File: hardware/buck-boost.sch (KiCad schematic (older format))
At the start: 60 parts, among them J1 FC681465, J2 Screw_Terminal_1x02, J3 Screw_Terminal_1x02, J4 DS1013-20S, J5 PLS-2, Q1 IRLML0030TRPBF, SW1 SW_Push, U1 L78L33_SOT89, Y1 Crystal

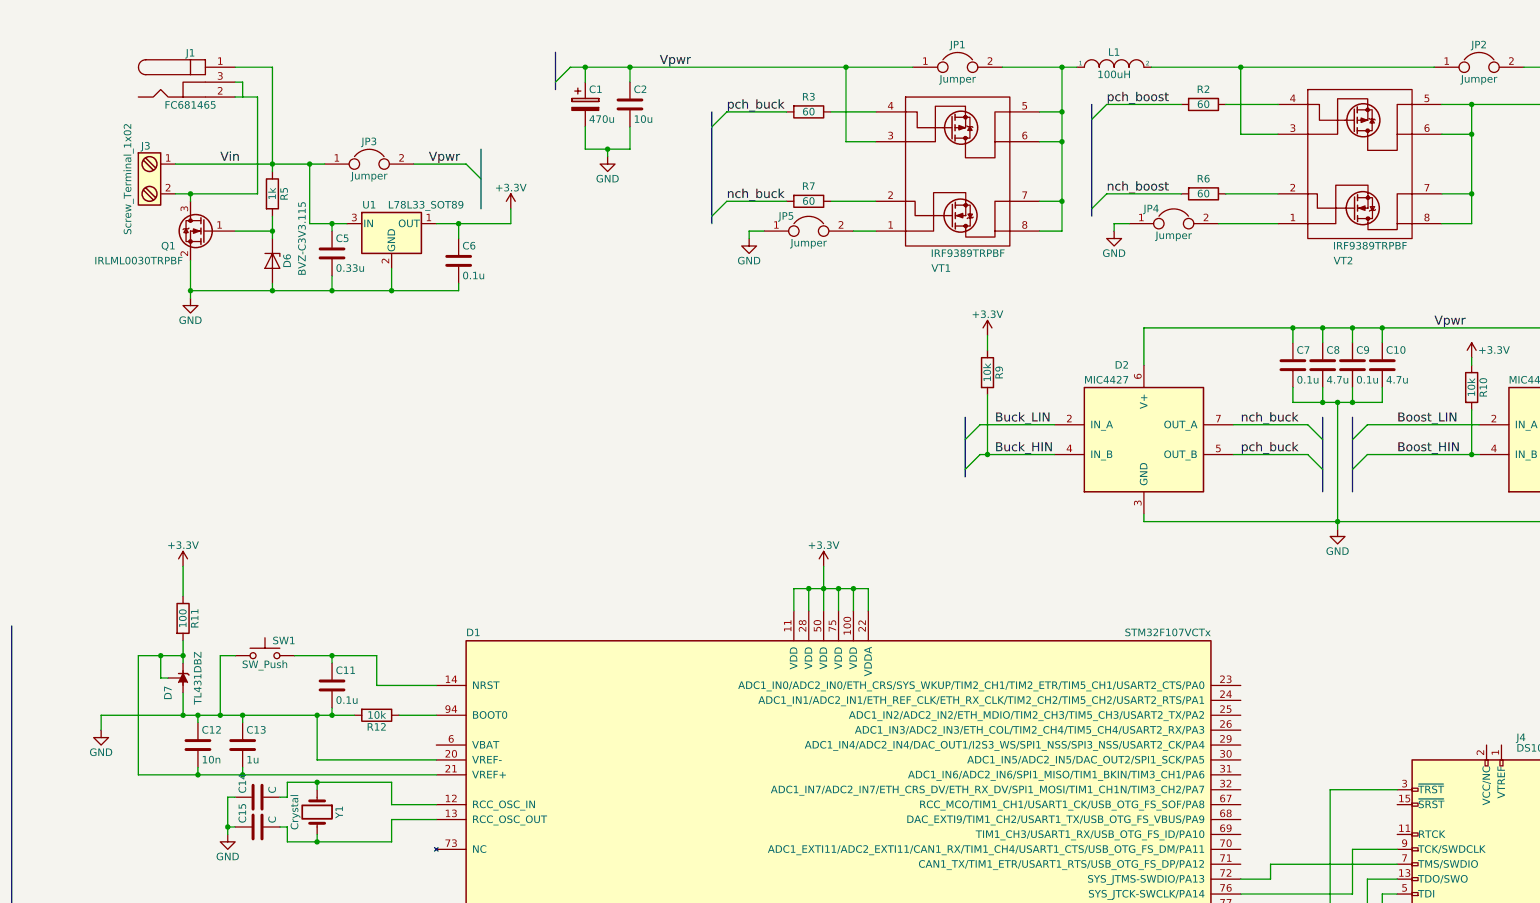
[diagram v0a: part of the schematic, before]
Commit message: fix schematic + set footprints
fix a few issues in schematic and set footprints for all components
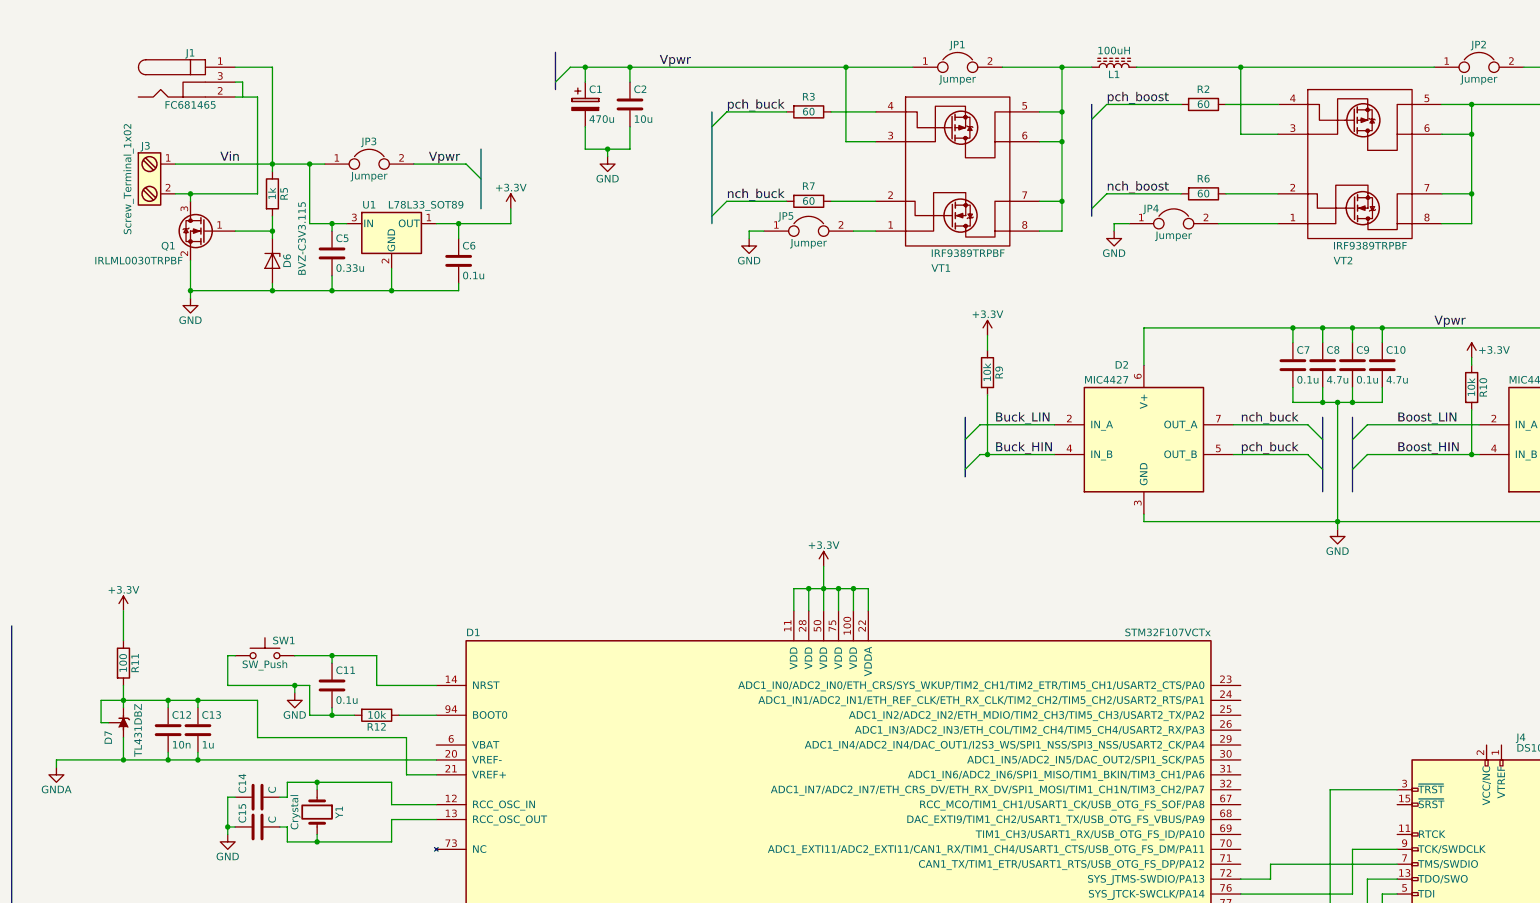
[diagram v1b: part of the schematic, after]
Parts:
- removed L1: 100uH, symbol INDUCTOR
- added L1: 100uH, Inductors_SMD:INDUCTOR_Bourns_SDR1307, symbol L_Core_Ferrite
- C1, C3: footprint (none) -> Capacitors_THT:CP_Radial_D10.0mm_P5.00mm
- C10, C23, C8: footprint (none) -> Capacitors_SMD:C_1206_HandSoldering
- C11, C12, C13, C14, C15, C16, C17, C18, C19, C20, C21, C22, C5, C6, C7, C9: footprint (none) -> Capacitors_SMD:C_0603_HandSoldering
- C2, C4: footprint (none) -> Capacitors_SMD:C_1210_HandSoldering
- D1: footprint LQFP100 -> Housings_QFP:LQFP-100_14x14mm_Pitch0.5mm
- D2, D3: footprint (none) -> Housings_SOIC:SOIC-8_3.9x4.9mm_Pitch1.27mm
- D4: footprint Package_TO_SOT_SMD:SOT-23-5 -> TO_SOT_Packages_SMD:SOT-23-5_HandSoldering
- D5: footprint TO_SOT_Packages_SMD:SOT-23-5 -> TO_SOT_Packages_SMD:SOT-23-5_HandSoldering
- D6: footprint (none) -> Diodes_SMD:D_1206
- D7, Q1: footprint Package_TO_SOT_SMD:SOT-23 -> TO_SOT_Packages_SMD:SOT-23
- J1: footprint (none) -> Connectors:BARREL_JACK
- J2, J3: footprint (none) -> TerminalBlock_Phoenix:TerminalBlock_Phoenix_MKDS1.5-2pol
- J4: footprint (none) -> Connectors:IDC_Header_Straight_20pins
- J5, JP1, JP2, JP3, JP4, JP5: footprint (none) -> Pin_Headers:Pin_Header_Straight_1x02_Pitch2.54mm
- R1: footprint (none) -> Resistors_SMD:R_1206_HandSoldering
- R10, R11, R12, R13, R4, R5, R8, R9: footprint (none) -> Resistors_SMD:R_0603_HandSoldering
- R2, R3, R6, R7: footprint (none) -> Resistors_SMD:R_0805_HandSoldering
- SW1: footprint (none) -> Buttons_Switches_THT:SW_PUSH_6mm
- U1: footprint Package_TO_SOT_SMD:SOT-89-3 -> TO_SOT_Packages_SMD:SOT-89-3_Handsoldering
- VT1, VT2: footprint Housings_SOIC:SO-8_5.3x6.2mm_Pitch1.27mm -> Housings_SOIC:SOIC-8_3.9x4.9mm_Pitch1.27mm
- Y1: footprint (none) -> Crystals:Crystal_HC49-U_Vertical
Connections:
- net GND: no longer C12.1, C13.1, D1.20 (VREF-), D7.3 (A)
- net GNDA: now also C12.2, C13.2, D1.20 (VREF-), D7.3 (A)
- net at JP1.2, VT1.5 (D2), VT1.6 (D2)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: now also L1.1
- net at JP2.1, VT2.3 (S2): now also L1.2
- net at D1.21 (VREF+), D7.1 (K), D7.2 (REF)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: now also C12.1, C13.1; no longer C12.2, C13.2
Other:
- moved on the sheet: C12, C13, D7, R11

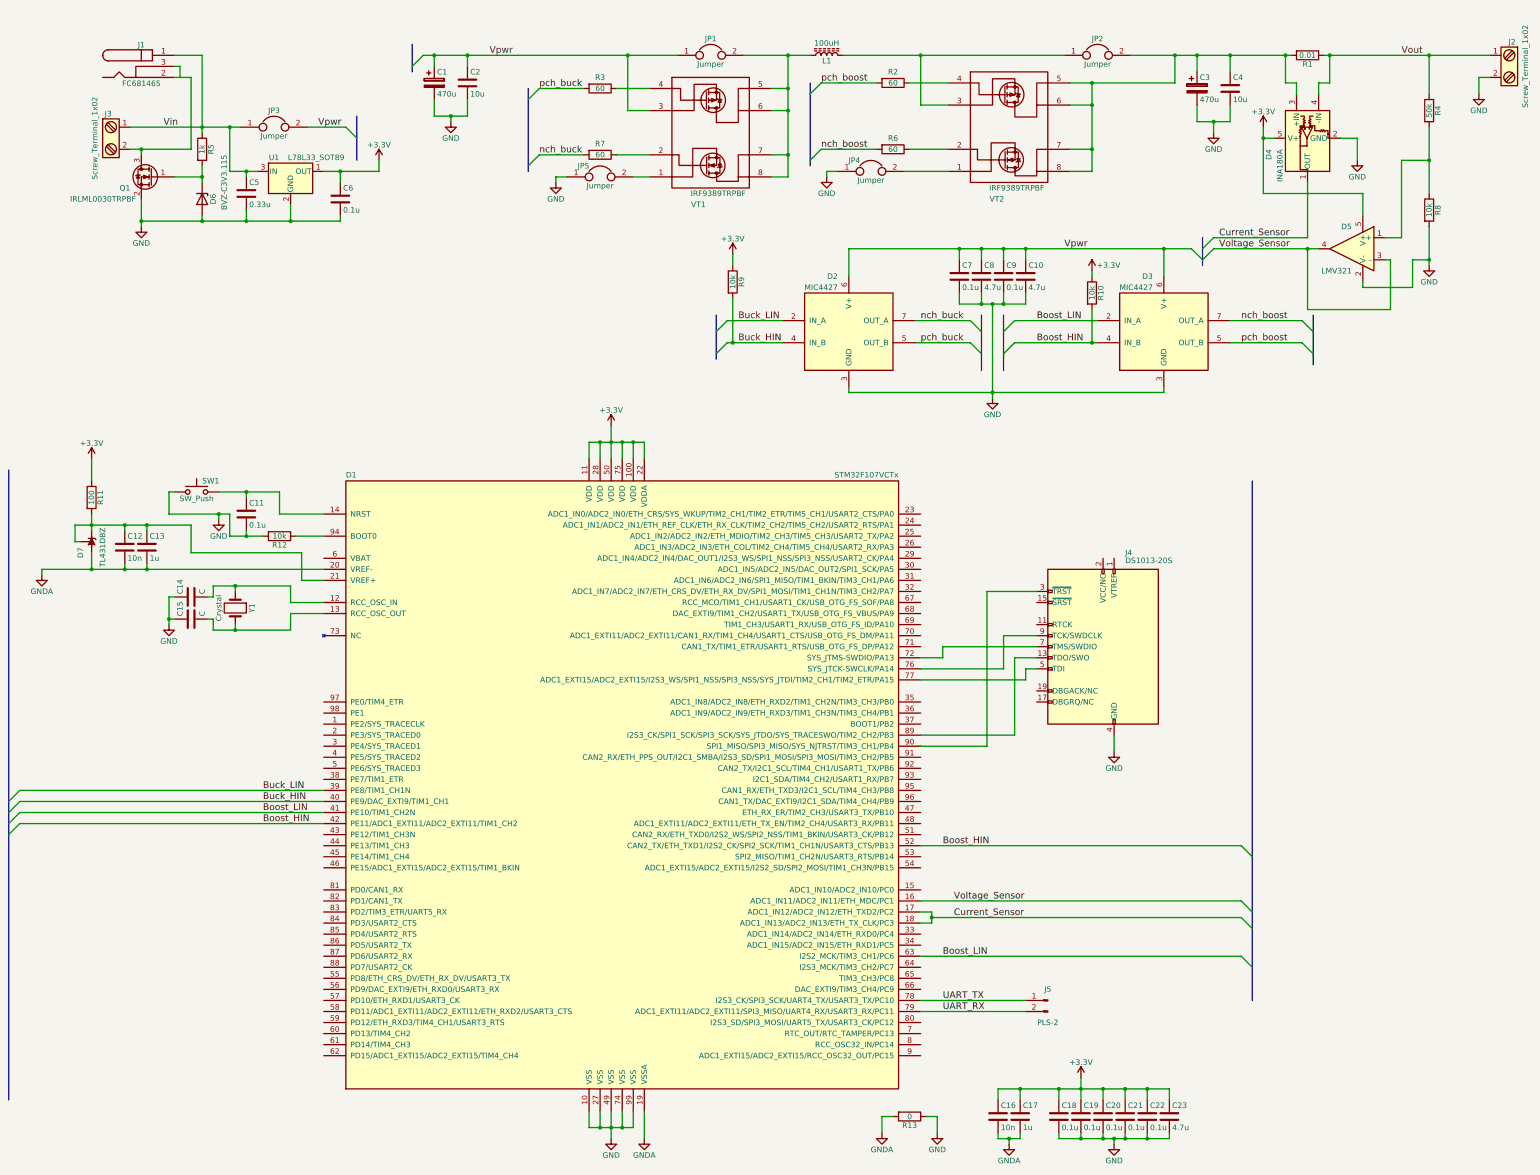
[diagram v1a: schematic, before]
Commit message: add pcb to project(first version) and schematic changes
Schematic
1. Test points added
2. Reset button and GNDA deleted
3. Voltage and Current sensors inputs on MCU (D1) was changed for better PCB design
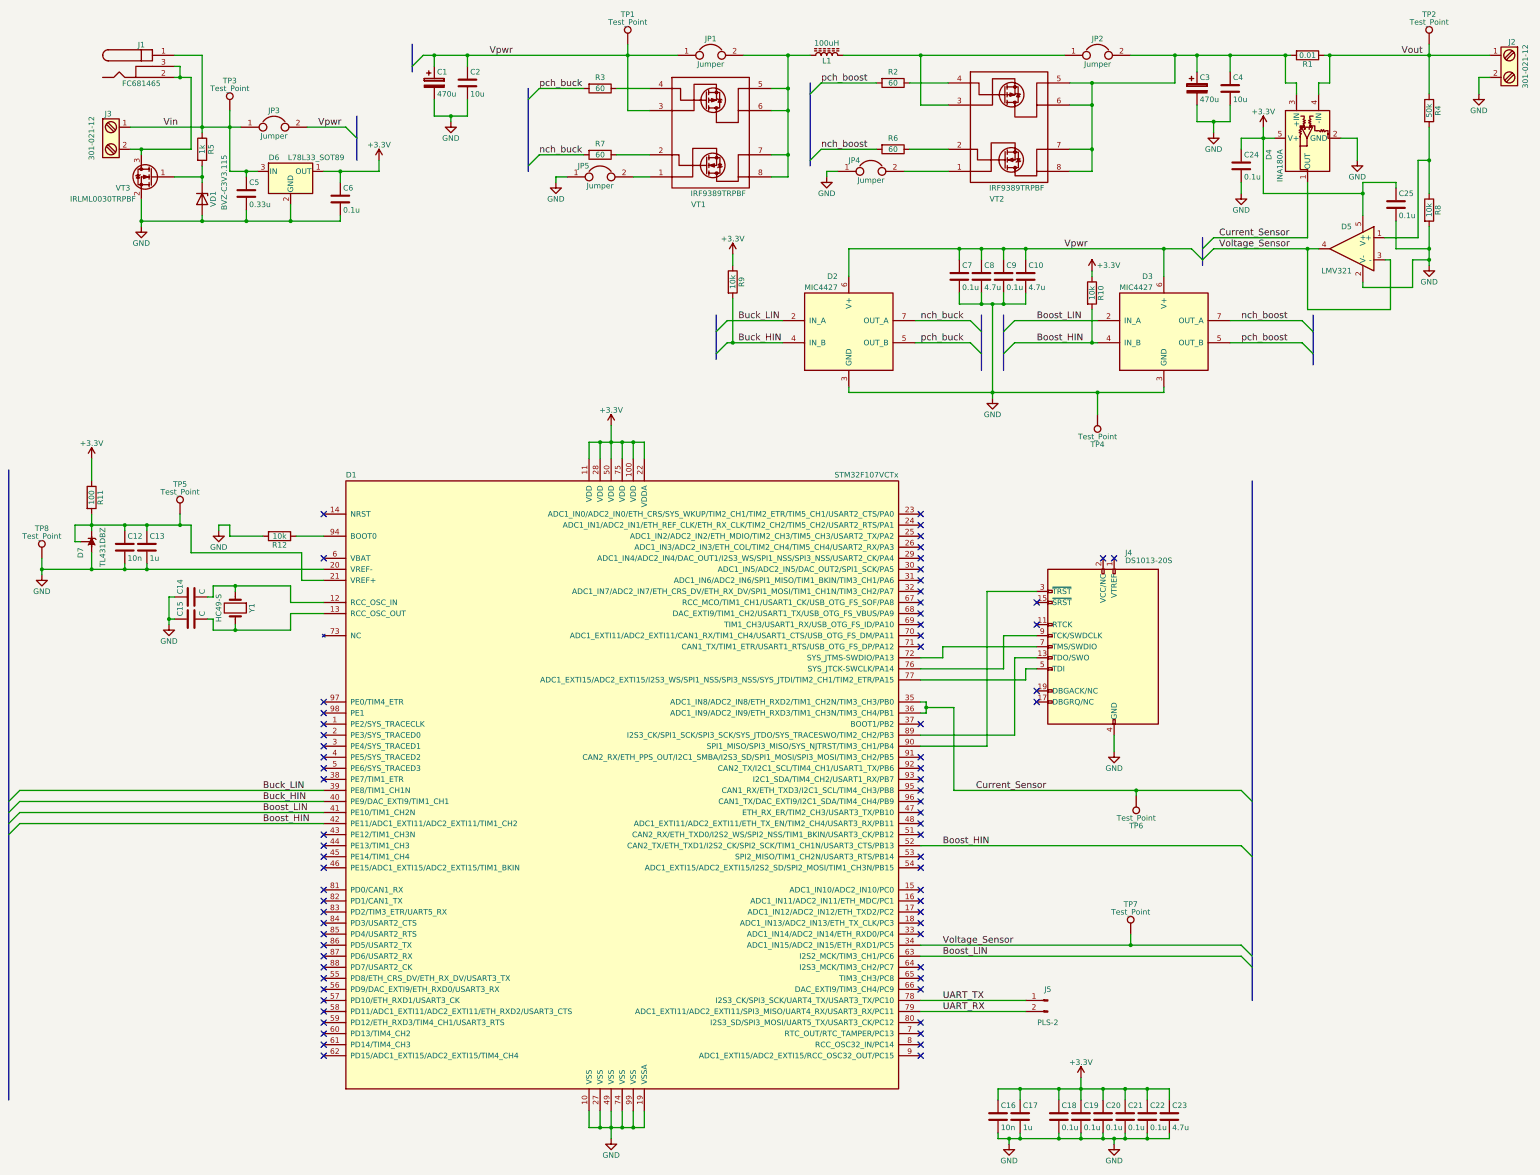
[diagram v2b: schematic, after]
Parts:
- removed C11: 0.1u, Capacitors_SMD:C_0603_HandSoldering, symbol C
- removed R13: 0, Resistors_SMD:R_0603_HandSoldering, symbol R
- removed SW1: SW_Push, Buttons_Switches_THT:SW_PUSH_6mm, symbol SW_Push
- added C24, C25: 0.1u, Capacitors_SMD:C_0603_HandSoldering, symbol C
- added TP1, TP2, TP3, TP5, TP6, TP7: Test_Point, Measurement_Points:Measurement_Point_Round-SMD-Pad_Small, symbol Test_Point
- added TP4, TP8: Test_Point, Measurement_Points:Measurement_Point_Round-TH_Big, symbol Test_Point
- J2, J3: value Screw_Terminal_1x02 -> 301-021-12
- Y1: value Crystal -> HC49-S
- renumbered U1 to D6, D6 to VD1, Q1 to VT3
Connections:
- net GNDA is gone; now on net GND: C12.2, C13.2, C16.2, C17.2, D1.19 (VSSA), D1.20 (VREF-), D7.3 (A)
- net +3V3: now also C24.1, C25.1
- net Current_Sensor: now also D1.35 (ADC1_IN8/ADC2_IN8/ETH_RXD2/TIM1_CH2N/TIM3_CH3/PB0), D1.36 (ADC1_IN9/ADC2_IN9/ETH_RXD3/TIM1_CH3N/TIM3_CH4/PB1), TP6.1; no longer D1.17 (ADC1_IN12/ADC2_IN12/ETH_TXD2/PC2), D1.18 (ADC1_IN13/ADC2_IN13/ETH_TX_CLK/PC3)
- net GND: now also C24.2, C25.2, TP4.1, TP8.1
- net Vin: now also TP3.1
- net Voltage_Sensor: now also D1.34 (ADC1_IN15/ADC2_IN15/ETH_RXD1/PC5), TP7.1; no longer D1.16 (ADC1_IN11/ADC2_IN11/ETH_MDC/PC1)
- net Vout: now also TP2.1
- net Vpwr: now also TP1.1
- net at C12.1, C13.1, D1.21 (VREF+)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: now also TP5.1
- net at J1.2, J3.2, VT3.3 (D): now also J1.3
- no-connect marks 0 -> 72

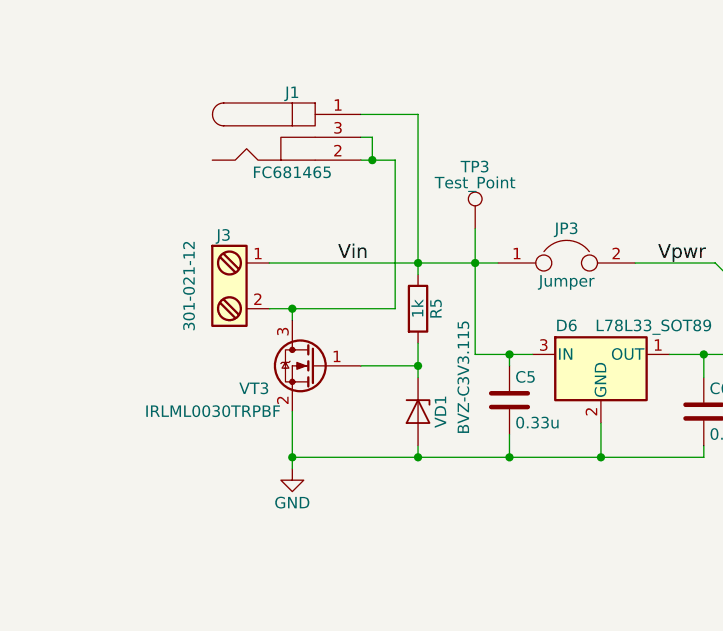
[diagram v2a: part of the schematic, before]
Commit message: change reverse polarity protection from low side to high side
1. polarity protection schematic changes
2. new tracing for analog gnd part of pcb (gnda still not in shematic)
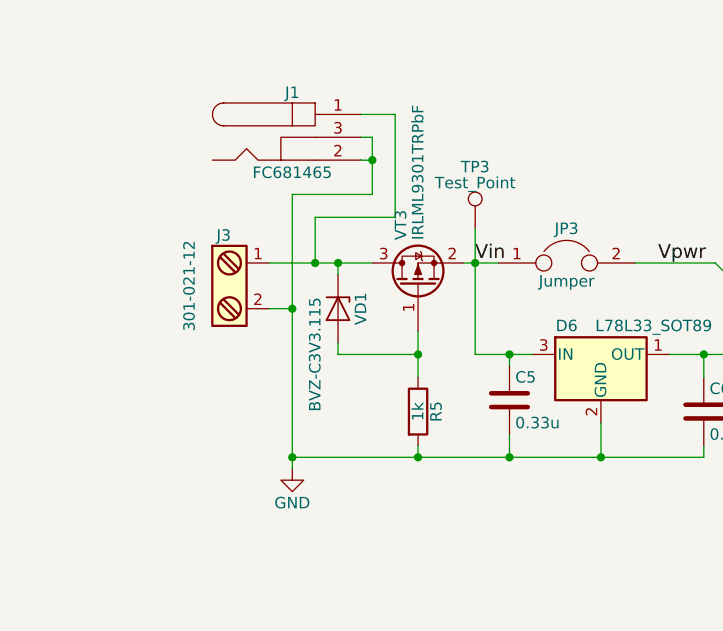
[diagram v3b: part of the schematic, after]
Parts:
- removed VT3: IRLML0030TRPBF, TO_SOT_Packages_SMD:SOT-23, symbol IRLML0030TRPBF
- added VT3: IRLML9301TRPbF, TO_SOT_Packages_SMD:SOT-23, symbol IRLML9301TRPbF
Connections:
- net GND: now also J1.2, J1.3, J3.2, R5.2; no longer VD1.2 (A)
- net Vin: now also VT3.2 (S); no longer J1.1, J3.1, R5.1
- net at VD1.1 (K): now also J1.1, J3.1, VT3.3 (D); no longer R5.2
- new net: R5.1, VD1.2 (A), VT3.1 (G)
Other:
- moved on the sheet: R5, VD1
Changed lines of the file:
@@
-$EndComp
-$Comp
-L IRLML0030TRPBF VT3
-U 1 1 5AA35423
-P 1900 2150
-F 0 "VT3" H 2100 2050 50  0000 L CNN
-F 1 "IRLML0030TRPBF" H 2050 1950 50  0000 L CNN
-F 2 "TO_SOT_Packages_SMD:SOT-23" H 2100 2075 50  0001 L CIN
-F 3 "" H 1900 2150 50  0001 L CNN
-	1    1900 2150
-	-1   0    0    -1
 $EndComp
 $Comp
 L R R5
 U 1 1 5AA357E9
-P 2350 1900
-F 0 "R5" V 2430 1900 50  0000 C CNN
-F 1 "1k" V 2350 1900 50  0000 C CNN
-F 2 "Resistors_SMD:R_0603_HandSoldering" V 2280 1900 50  0001 C CNN
-F 3 "" H 2350 1900 50  0001 C CNN
-	1    2350 1900
+P 2350 2350
+F 0 "R5" V 2430 2350 50  0000 C CNN
+F 1 "1k" V 2350 2350 50  0000 C CNN
+F 2 "Resistors_SMD:R_0603_HandSoldering" V 2280 2350 50  0001 C CNN
+F 3 "" H 2350 2350 50  0001 C CNN
+	1    2350 2350
 	1    0    0    -1
 $EndComp
@@
 L D_Zener VD1
 U 1 1 5AA3585C
-P 2350 2350
-F 0 "VD1" H 2350 2450 50  0000 C CNN
-F 1 "BVZ-C3V3.115" H 2200 2550 50  0000 C CNN
-F 2 "Diodes_SMD:D_1206" H 2350 2350 50  0001 C CNN
-F 3 "" H 2350 2350 50  0001 C CNN
-	1    2350 2350
+P 2000 1900
+F 0 "VD1" H 2000 2000 50  0000 C CNN
+F 1 "BVZ-C3V3.115" H 2200 1800 50  0000 C CNN
+F 2 "Diodes_SMD:D_1206" H 2000 1900 50  0001 C CNN
+F 3 "" H 2000 1900 50  0001 C CNN
+	1    2000 1900
 	0    1    1    0
 $EndComp
@@
 Text Label 3400 1700 0    60   ~ 0
 Vpwr
-Text Label 2000 1700 0    60   ~ 0
+Text Label 2600 1700 0    60   ~ 0
 Vin
 Text Label 13200 1050 0    60   ~ 0
@@
 	4350 1050 6650 1050
 Wire Wire Line
-	1700 1700 2700 1700
-Wire Wire Line
-	1700 1900 2250 1900
-Wire Wire Line
-	1800 1900 1800 1950
-Wire Wire Line
-	1800 2350 1800 2600
-Wire Wire Line
-	2350 2050 2350 2200
-Wire Wire Line
-	2350 1050 2350 1750
-Connection ~ 2350 1700
-Wire Wire Line
-	2350 2150 2100 2150
-Connection ~ 2350 2150
+	1800 1400 1800 2600
 Wire Wire Line
 	2350 2500 2350 2550
@@
 	13900 1250 13900 1400
 Wire Wire Line
-	2100 1050 2350 1050
-Wire Wire Line
 	2150 1150 2100 1150
-Wire Wire Line
-	2250 1900 2250 1250
 Connection ~ 1800 1900
 Wire Wire Line
@@
 Connection ~ 1850 5300
 Wire Wire Line
-	2250 1250 2100 1250
-Wire Wire Line
-	2150 1150 2150 1250
+	2150 1150 2150 1400
 Connection ~ 2150 1250
 Wire Wire Line
@@
 $EndComp
 Connection ~ 900  5700
+Wire Wire Line
+	1700 1900 1800 1900
+Wire Wire Line
+	2150 1250 2100 1250
+Wire Wire Line
+	2150 1400 1800 1400
+Wire Wire Line
+	2100 1050 2250 1050
+Wire Wire Line
+	2250 1050 2250 1500
+Wire Wire Line
+	2250 1500 1900 1500
+Wire Wire Line
+	1900 1500 1900 1700
+Connection ~ 1900 1700
+$Comp
+L IRLML9301TRPbF VT3
+U 1 1 5AA6F8D3
+P 2350 1800
+F 0 "VT3" H 2550 1875 50  0000 L CNN
+F 1 "IRLML9301TRPbF" H 2550 1800 50  0000 L CNN
+F 2 "TO_SOT_Packages_SMD:SOT-23" H 2550 1725 50  0001 L CIN
+F 3 "" H 2350 1800 50  0001 L CNN
+	1    2350 1800
+	0    -1   -1   0
+$EndComp
+Wire Wire Line
+	2550 1700 2700 1700
+Wire Wire Line
+	1700 1700 2150 1700
+Connection ~ 2000 1700
+Wire Wire Line
+	2000 1750 2000 1700
+Wire Wire Line
+	2000 2050 2000 2100
+Wire Wire Line
+	2000 2100 2350 2100
+Wire Wire Line
+	2350 2000 2350 2200
+Connection ~ 2350 2100
 $EndSCHEMATC
